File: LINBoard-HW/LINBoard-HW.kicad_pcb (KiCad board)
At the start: 4 copper layers, 46 x 56 mm, 71 parts, among them J1 TC, J3 USB_C_Receptacle_USB2.0, J4 ATM15-6P-BM03, SW1 BOOT, SW2 RESET, SW3 MASTER, U1 PCA82C250, U2 TJA1029T, U3 TPS56339DDC, U4 LD1117S33CTR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

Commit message: change pinout, export
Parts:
- U6: value STM32F302C8Tx -> STM32F302CCTx
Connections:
- J4 pad 4: GND -> LIN
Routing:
- net LIN: track 20.0 -> 26.3 mm
- net GND: vias 52 -> 48
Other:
- board text added: "1-CAN L 2-CAN H 3-LIN 4-LIN 5-GND 6-12V"
- board text removed: "1-CAN L 2-CAN H 3-LIN 4-GND 5-GND 6-12V"
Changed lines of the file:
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@@
 		(sheetname "/LIN/")
 		(sheetfile "LIN.kicad_sch")
-		(attr through_hole)
+		(attr through_hole exclude_from_bom)
 		(fp_line
 			(start -2.7 1.25)
@@
 		(sheetname "/Microcontroller/")
 		(sheetfile "Microcontroller.kicad_sch")
-		(attr through_hole)
+		(attr through_hole exclude_from_bom)
 		(fp_circle
 			(center 0 0)
@@
 		(sheetname "/Microcontroller/")
 		(sheetfile "Microcontroller.kicad_sch")
-		(attr through_hole)
+		(attr through_hole exclude_from_bom)
 		(fp_circle
 			(center 0 0)
@@
 		(sheetname "/Microcontroller/")
 		(sheetfile "Microcontroller.kicad_sch")
-		(attr through_hole)
+		(attr through_hole exclude_from_bom)
 		(fp_circle
 			(center 0 0)
@@
 		(sheetname "/Microcontroller/")
 		(sheetfile "Microcontroller.kicad_sch")
-		(attr through_hole)
+		(attr through_hole exclude_from_bom)
 		(fp_circle
 			(center 0 0)
@@
 		(sheetname "/Connectors/")
 		(sheetfile "Connectors.kicad_sch")
-		(attr through_hole)
+		(attr through_hole exclude_from_bom)
 		(fp_line
 			(start -1.62 2.4)
@@
 		(sheetname "/Microcontroller/")
 		(sheetfile "Microcontroller.kicad_sch")
-		(attr through_hole)
+		(attr through_hole exclude_from_bom)
 		(fp_circle
 			(center 0 0)
@@
 		(sheetname "/Microcontroller/")
 		(sheetfile "Microcontroller.kicad_sch")
-		(attr through_hole)
+		(attr through_hole exclude_from_bom)
 		(fp_circle
 			(center 0 0)
@@
 		(sheetfile "Microcontroller.kicad_sch")
 		(zone_connect 1)
-		(attr exclude_from_pos_files allow_soldermask_bridges)
+		(attr exclude_from_pos_files exclude_from_bom allow_soldermask_bridges)
 		(net_tie_pad_groups "1, 2")
 		(fp_poly
@@
 		(sheetfile "Power.kicad_sch")
 		(zone_connect 1)
-		(attr exclude_from_pos_files allow_soldermask_bridges)
+		(attr exclude_from_pos_files exclude_from_bom allow_soldermask_bridges)
 		(net_tie_pad_groups "1, 2")
 		(fp_poly
@@
 		(sheetfile "Microcontroller.kicad_sch")
 		(zone_connect 1)
-		(attr exclude_from_pos_files allow_soldermask_bridges)
+		(attr exclude_from_pos_files exclude_from_bom allow_soldermask_bridges)
 		(net_tie_pad_groups "1, 2")
 		(fp_poly
@@
 			)
 		)
-		(property "Value" "STM32F302C8Tx"
+		(property "Value" "STM32F302CCTx"
 			(at 0 5.85 90)
 			(layer "F.Fab")
@@
 		(sheetname "/Microcontroller/")
 		(sheetfile "Microcontroller.kicad_sch")
-		(attr through_hole)
+		(attr through_hole exclude_from_bom)
 		(fp_circle
 			(center 0 0)
@@
 		(sheetname "/Microcontroller/")
 		(sheetfile "Microcontroller.kicad_sch")
-		(attr through_hole)
+		(attr through_hole exclude_from_bom)
 		(fp_line
 			(start -2.7 -1.25)
@@
 		(sheetname "/Connectors/")
 		(sheetfile "Connectors.kicad_sch")
-		(attr smd)
+		(attr smd exclude_from_bom)
 		(fp_line
 			(start -15 -7)
@@
 			(layers "*.Cu" "*.Mask")
 			(remove_unused_layers no)
-			(net 2 "GND")
+			(net 1 "LIN")
 			(pinfunction "Pin_4")
 			(pintype "passive")
@@
 		(sheetname "/")
 		(sheetfile "LINBoard-HW.kicad_sch")
-		(attr through_hole)
+		(attr through_hole exclude_from_bom)
 		(fp_poly
 			(pts
@@
 		)
 	)
-	(gr_text "1-CAN L\n2-CAN H\n3-LIN\n4-GND\n5-GND\n6-12V"
+	(gr_text "1-CAN L\n2-CAN H\n3-LIN\n4-LIN\n5-GND\n6-12V"
 		(at -8.1 8.3 0)
 		(layer "B.SilkS")
@@
 	)
 	(segment
+		(start -4.2 12.35)
+		(end -5.2 13.35)
+		(width 0.4)
+		(layer "F.Cu")
+		(net 1)
+	)
+	(segment
 		(start -13.1 21.9)
 		(end -13.05 21.95)
@@
 	)
 	(segment
-		(start -4.2 12.35)
-		(end -4.2 16.15)
+		(start -5.2 13.35)
+		(end -5.2 17.15)
 		(width 0.4)
 		(layer "F.Cu")
@@
 	)
 	(segment
-		(start -4.2 16.15)
-		(end -5.2 17.15)
+		(start -5.2 17.15)
+		(end -6.584999 17.15)
 		(width 0.4)
 		(layer "F.Cu")
@@
 	)
 	(segment
-		(start -5.2 17.15)
-		(end -6.584999 17.15)
+		(start -4.2 6)
+		(end -4.2 12.35)
 		(width 0.4)
-		(layer "F.Cu")
+		(layer "In1.Cu")
 		(net 1)
 	)
@@
 	)
 	(via
-		(at -5 4)
-		(size 0.6)
-		(drill 0.35)
-		(layers "F.Cu" "B.Cu")
-		(free yes)
-		(net 2)
-	)
-	(via
-		(at -3.5 8)
-		(size 0.6)
-		(drill 0.35)
-		(layers "F.Cu" "B.Cu")
-		(free yes)
-		(net 2)
-	)
-	(via
 		(at -2.6 37)
 		(size 0.6)
@@
 	)
 	(via
-		(at -3.5 4)
-		(size 0.6)
-		(drill 0.35)
-		(layers "F.Cu" "B.Cu")
-		(free yes)
-		(net 2)
-	)
-	(via
 		(at 7.8 40.2)
 		(size 0.6)
@@
 		(net 2)
 	)
-	(via
-		(at -5 8)
-		(size 0.6)
-		(drill 0.35)
-		(layers "F.Cu" "B.Cu")
-		(free yes)
-		(net 2)
-	)

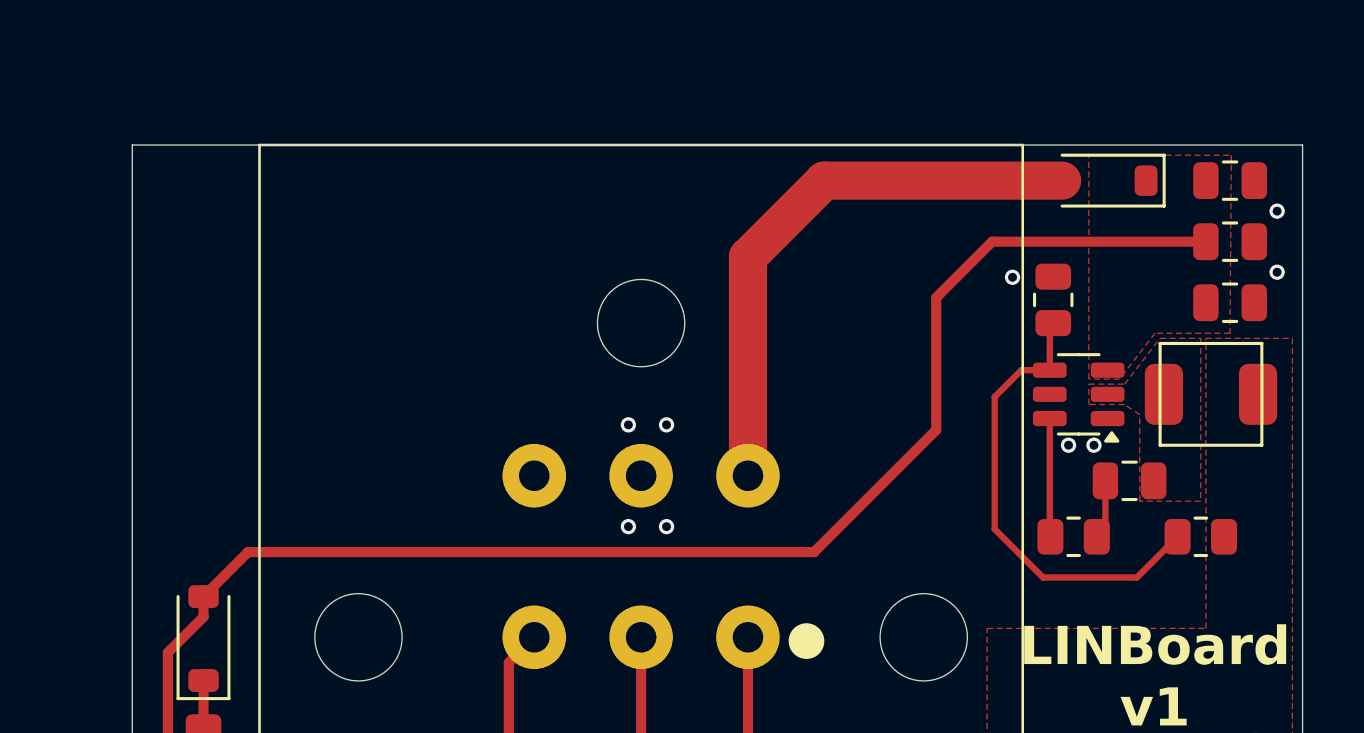
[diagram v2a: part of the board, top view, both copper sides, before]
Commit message: add tvs, fix reset button
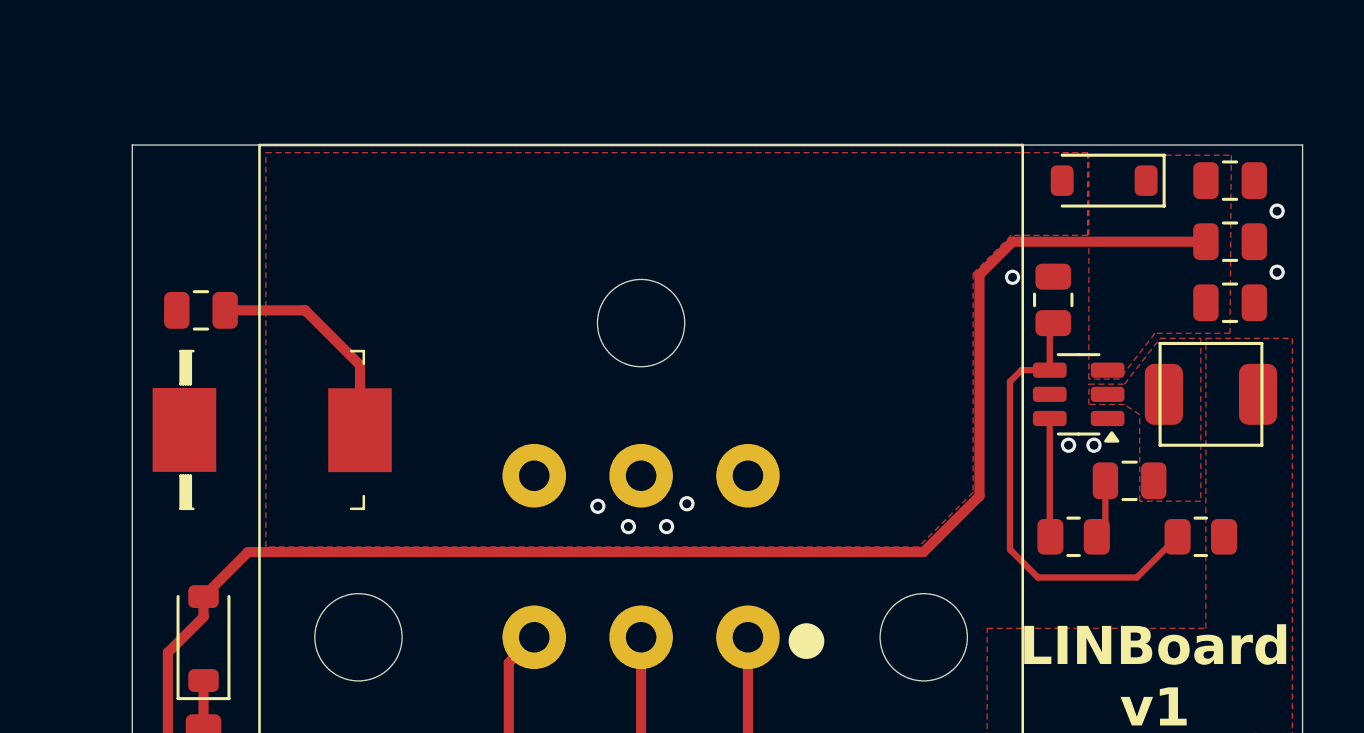
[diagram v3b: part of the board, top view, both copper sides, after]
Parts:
- added C6: 100nF, Capacitor_SMD:C_0805_2012Metric, F.Cu at (-17.3, -0.50)
- added D3: SMCJ16CA, digikey-footprints:DO-214AB_TVS, F.Cu at (-14.5, 4.20)
- J4: value ATM15-6P-BM03 -> ATM13-6P-BM04
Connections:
- SW2 pad 1: GND -> /Microcontroller/NRST
- SW2 pad 3: (no net) -> GND
- SW2 pad 4: (no net) -> GND
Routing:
- net +12V: track 22.2 -> 8.75 mm
- net +12P: track 77.9 -> 79.9 mm
- added copper zone on F.Cu, net +12V

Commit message: add button trace
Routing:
- net /Microcontroller/NRST: track 28.7 -> 34.7 mm
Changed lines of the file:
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@@
+	)
+	(segment
+		(start 14.8 46.25)
+		(end 20.8 46.25)
+		(width 0.15)
+		(layer "F.Cu")
+		(net 5)
 	)
 	(segment
